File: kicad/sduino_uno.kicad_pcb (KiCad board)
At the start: 2 copper layers, 68.6 x 53.3 mm, 51 parts, among them J1 Conn_01x04, J2 Conn_01x02, Q1 FDN340P, U1 NCP1117-5.0_SOT223, U2 NCP1117-3.3_SOT223, U3 CH340G, U4 STM8S105K_LQFP32, U5 LM358, U6 STM8S105K_UFQFPN32, X1 Jack-DC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

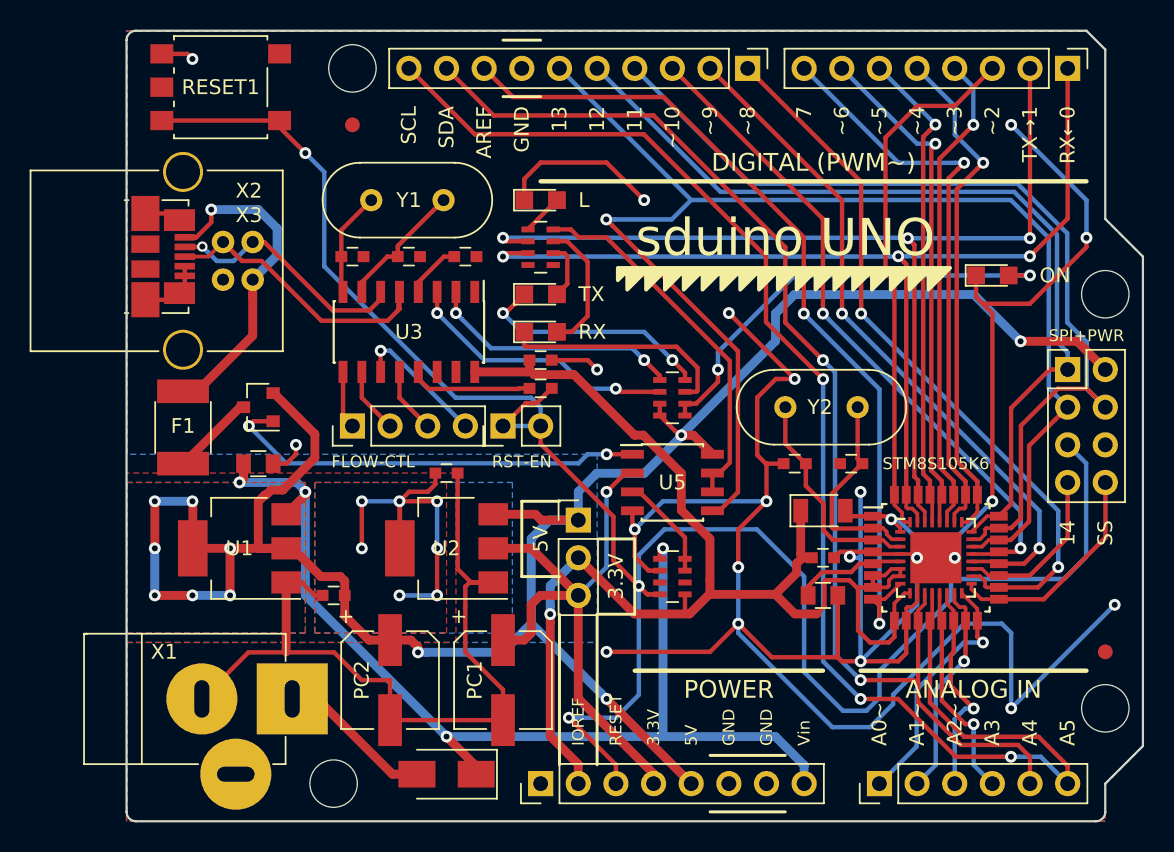
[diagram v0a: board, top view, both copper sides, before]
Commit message: revision 2017-10-08 - fix major error in TX/RX wiring (LEDs were connected in series) - improve ground fill surrounding crystals - rename IO14 to IO23 - add some pin numbers on the back side - update documentation
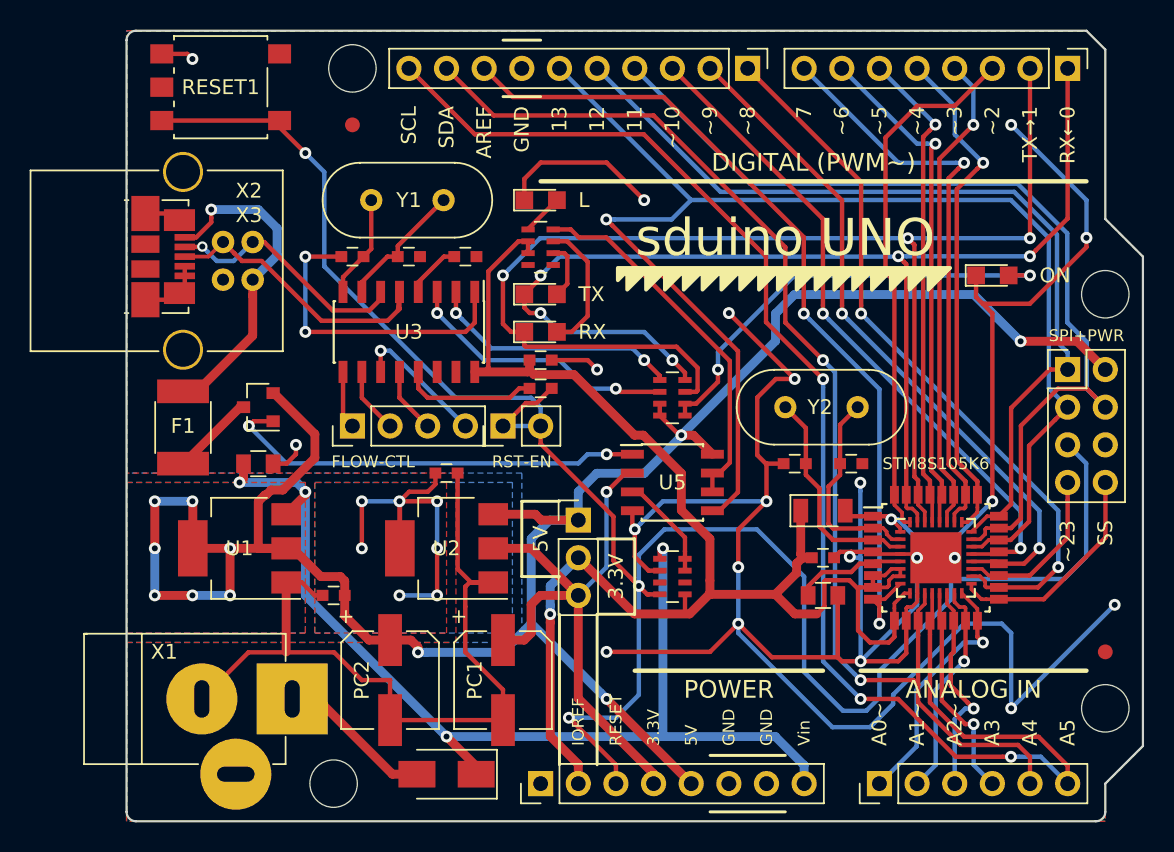
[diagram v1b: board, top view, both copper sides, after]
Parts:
- turned C2 to 180 degrees
- turned C5 to 180 degrees
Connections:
- net /IO14 renamed /IO23
- net /SS renamed /IO24/SS
- LED_RX1 pad 1: Net-(LED_RX1-Pad1) -> /IO1/TX
- LED_TX1 pad 1: Net-(LED_TX1-Pad1) -> /IO0/RX
- RN2 pad 2: /IO1/TX -> /MCUVCC
- RN2 pad 3: /IO0/RX -> /MCUVCC
- RN3 pad 7: Net-(LED_RX1-Pad1) -> /IO1/TX
- RN3 pad 8: Net-(LED_TX1-Pad1) -> /IO0/RX
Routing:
- net GND: track 264.6 -> 286.5 mm, vias 21 -> 23
- net /IO1/TX: track 68.4 -> 88.3 mm
- net Net-(LED_TX1-Pad1): track 16.4 -> 0.00 mm, vias 2 -> 0
- net Net-(LED_RX1-Pad1): track 15.6 -> 0.00 mm
- net /IO0/RX: track 69.8 -> 81.7 mm, vias 3 -> 5
- net /MCUVCC: track 92.4 -> 104.2 mm
- net Net-(C10-Pad1): track 8.26 -> 9.15 mm
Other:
- board text added: "15"
- board text added: "16"
- board text added: "17"
- board text added: "18"
- board text added: "19"
- board text added: "2017-10-08"
- board text added: "22"
- board text added: "24"
- board text added: "~~23"
- board text removed: "2017-10-01"

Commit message: board revision 2017-10-10 (minor PCB changes) - optimized ground fills - reduced thermal relief around the regulators' thermal pads
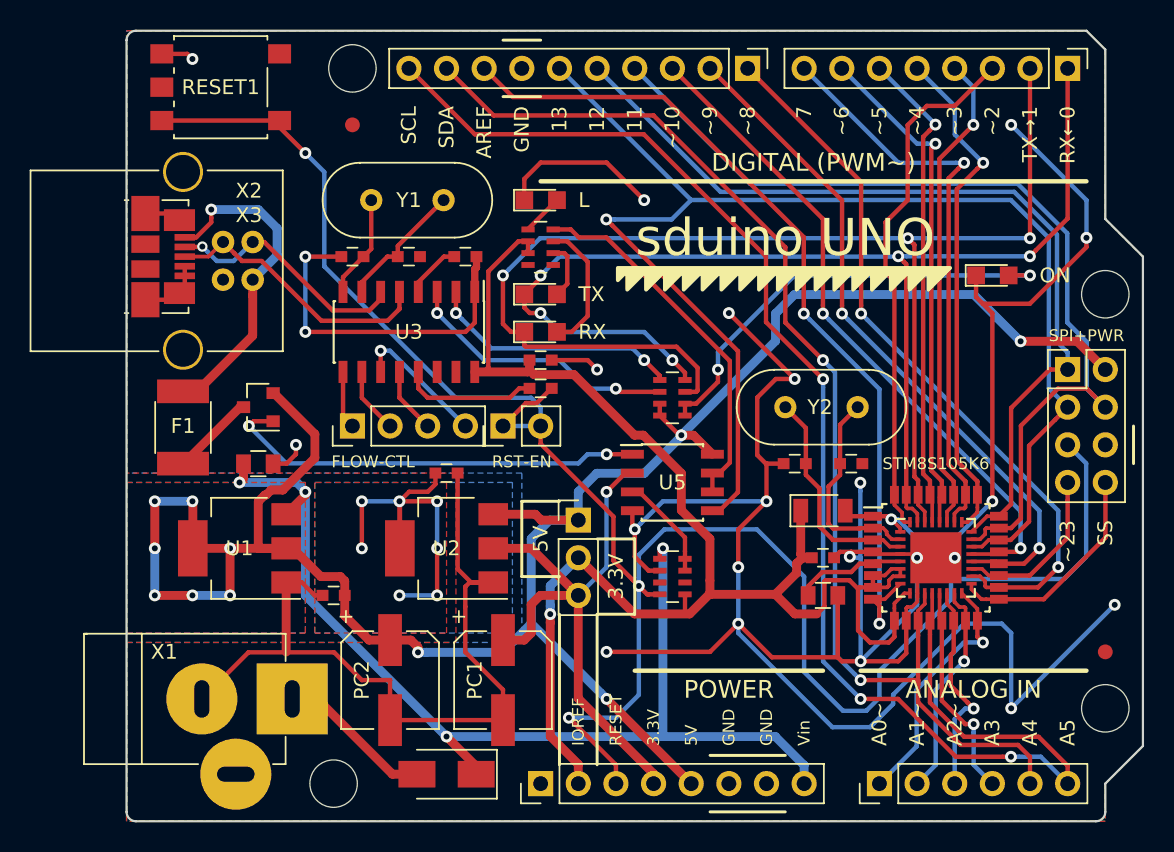
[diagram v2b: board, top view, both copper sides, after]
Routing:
- net GND: track 286.5 -> 288.9 mm
- net /D+: track 20.0 -> 18.7 mm
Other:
- board text added: "2017-10-10"
- board text removed: "2017-10-08"
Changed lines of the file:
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@@
     (area 114.224999 76.124999 182.955001 129.615001)
     (thickness 1.6)
-    (drawings 111)
-    (tracks 916)
+    (drawings 112)
+    (tracks 920)
     (zones 0)
     (modules 51)
@@
     (title "sduino UNO")
     (date 2017-09-15)
-    (rev 2017-10-08)
+    (rev 2017-10-10)
     (company "Benedikt Freisen")
     (comment 1 "see http://creativecommons.org/licenses/by-sa/2.5/")
@@
     (mod_text_size 1 1)
     (mod_text_width 0.15)
-    (pad_size 1.725 1.725)
+    (pad_size 2 3.8)
     (pad_drill 0)
     (pad_to_mask_clearance 0.2)
@@
     (visible_elements FFFFFF7F)
     (pcbplotparams
-      (layerselection 0x00030_80000001)
+      (layerselection 0x010f0_80000001)
       (usegerberextensions false)
       (excludeedgelayer true)
@@
       (outputformat 1)
       (mirror false)
-      (drillshape 1)
+      (drillshape 0)
       (scaleselection 1)
-      (outputdirectory ""))
+      (outputdirectory gerber))
   )
   (net 0 "")
@@
     (fp_line (start 1.85 -3.35) (end 1.85 3.35) (layer F.Fab) (width 0.1))
     (pad 2 smd rect (at 3.15 0 180) (size 2 3.8) (layers F.Cu F.Paste F.Mask)
-      (net 14 +5V))
+      (net 14 +5V) (thermal_width 1.2))
     (pad 2 smd rect (at -3.15 0 180) (size 2 1.5) (layers F.Cu F.Paste F.Mask)
       (net 14 +5V))
@@
     (fp_line (start 1.85 -3.35) (end 1.85 3.35) (layer F.Fab) (width 0.1))
     (pad 2 smd rect (at 3.15 0 180) (size 2 3.8) (layers F.Cu F.Paste F.Mask)
-      (net 15 +3V3))
+      (net 15 +3V3) (thermal_width 1.2))
     (pad 2 smd rect (at -3.15 0 180) (size 2 1.5) (layers F.Cu F.Paste F.Mask)
       (net 15 +3V3))
@@
     )
   )
+  (gr_line (start 182.245 102.87) (end 182.245 105.41) (layer F.SilkS) (width 0.2))
   (gr_text 19 (at 133.35 80.645) (layer B.SilkS)
     (effects (font (size 1 1) (thickness 0.15)) (justify mirror))
@@
     (effects (font (size 1 1) (thickness 0.15)) (justify left mirror))
   )
-  (gr_text 2017-10-08 (at 171.45 91.44) (layer B.SilkS)
+  (gr_text 2017-10-10 (at 171.45 91.44) (layer B.SilkS)
     (effects (font (size 1.5 1.5) (thickness 0.3)) (justify left mirror))
   )
@@
   (gr_line (start 114.935 129.54) (end 179.705 129.54) (layer Edge.Cuts) (width 0.15))
   (gr_line (start 114.3 76.835) (end 114.3 128.905) (layer Edge.Cuts) (width 0.15))
+  (segment (start 137.91 92.176048) (end 137.91 91.44) (width 0.5) (layer F.Cu) (net 1))
+  (segment (start 137.795 92.291048) (end 137.91 92.176048) (width 0.5) (layer F.Cu) (net 1))
+  (segment (start 137.795 93.82) (end 137.795 92.291048) (width 0.5) (layer F.Cu) (net 1))
   (segment (start 163.814278 111.744278) (end 163.814278 107.261686) (width 0.3) (layer B.Cu) (net 1))
   (segment (start 163.814278 107.261686) (end 163.814278 106.696001) (width 0.3) (layer B.Cu) (net 1))
@@
   (via (at 171.457525 122.984562) (size 0.8) (drill 0.4) (layers F.Cu B.Cu) (net 24))
   (segment (start 171.457525 125.737525) (end 171.457525 123.550247) (width 0.3) (layer B.Cu) (net 24))
+  (segment (start 163.83 120.015) (end 167.71 120.015) (width 0.3) (layer F.Cu) (net 25))
+  (segment (start 167.71 120.015) (end 167.71 120.331982) (width 0.3) (layer F.Cu) (net 25))
   (segment (start 168.16 114.16) (end 168.16 114.874998) (width 0.25) (layer F.Cu) (net 25))
   (segment (start 168.16 114.874998) (end 167.71 115.324998) (width 0.25) (layer F.Cu) (net 25))
@@
   (segment (start 162.09934 99.23434) (end 162.09934 118.28434) (width 0.3) (layer B.Cu) (net 25))
   (segment (start 163.430001 119.615001) (end 163.83 120.015) (width 0.3) (layer B.Cu) (net 25))
-  (segment (start 163.83 120.015) (end 167.393018 120.015) (width 0.3) (layer F.Cu) (net 25))
-  (segment (start 167.393018 120.015) (end 167.71 120.331982) (width 0.3) (layer F.Cu) (net 25))
   (via (at 163.83 120.015) (size 0.8) (drill 0.4) (layers F.Cu B.Cu) (net 25))
   (segment (start 158.75 95.885) (end 161.29 98.425) (width 0.3) (layer F.Cu) (net 25))
@@
   (segment (start 165.1 115) (end 164.66 114.56) (width 0.3) (layer F.Cu) (net 33))
   (via (at 165.1 116.205) (size 0.8) (drill 0.4) (layers F.Cu B.Cu) (net 33))
-  (segment (start 166.11 107.51) (end 166.11 93.099533) (width 0.3) (layer F.Cu) (net 34))
-  (segment (start 166.11 93.099533) (end 165.51 92.499533) (width 0.3) (layer F.Cu) (net 34))
-  (segment (start 165.51 92.499533) (end 165.51 83.41) (width 0.3) (layer F.Cu) (net 34))
-  (segment (start 165.51 83.41) (end 167.650509 81.269491) (width 0.3) (layer F.Cu) (net 34))
-  (segment (start 167.650509 81.269491) (end 170.190509 81.269491) (width 0.3) (layer F.Cu) (net 34))
-  (segment (start 170.190509 81.269491) (end 172.72 78.74) (width 0.3) (layer F.Cu) (net 34))
+  (segment (start 165.51 92.499533) (end 166.11 93.099533) (width 0.3) (layer F.Cu) (net 34))
+  (segment (start 165.51 89.125) (end 165.51 92.499533) (width 0.3) (layer F.Cu) (net 34))
+  (segment (start 167.005 87.63) (end 165.51 89.125) (width 0.3) (layer F.Cu) (net 34))
+  (segment (start 167.005 82.563709) (end 167.005 87.63) (width 0.3) (layer F.Cu) (net 34))
+  (segment (start 166.11 93.099533) (end 166.11 107.51) (width 0.3) (layer F.Cu) (net 34))
+  (segment (start 168.299218 81.269491) (end 167.005 82.563709) (width 0.3) (layer F.Cu) (net 34))
+  (segment (start 170.190509 81.269491) (end 168.299218 81.269491) (width 0.3) (layer F.Cu) (net 34))
+  (segment (start 172.72 78.74) (end 170.190509 81.269491) (width 0.3) (layer F.Cu) (net 34))
   (segment (start 172.747499 78.767499) (end 172.72 78.74) (width 0.3) (layer F.Cu) (net 34))
   (segment (start 167.16 109.36) (end 166.785 109.36) (width 0.25) (layer F.Cu) (net 34))
@@
   (segment (start 132.715 94.97) (end 131.914988 95.770012) (width 0.3) (layer F.Cu) (net 58))
   (segment (start 122.089999 91.734999) (end 121.569999 91.214999) (width 0.3) (layer F.Cu) (net 58))
-  (segment (start 132.614999 95.070001) (end 132.715 93.82) (width 0.3) (layer F.Cu) (net 58))
   (segment (start 123.414801 91.734999) (end 122.089999 91.734999) (width 0.3) (layer F.Cu) (net 58))
   (segment (start 132.715 93.82) (end 132.715 94.97) (width 0.3) (layer F.Cu) (net 58))
@@
     (min_thickness 0.254)
     (keepout (tracks allowed) (vias allowed) (copperpour not_allowed))
-    (fill (arc_segments 16) (thermal_gap 0.508) (thermal_bridge_width 0.508))
+    (fill yes (arc_segments 16) (thermal_gap 0.508) (thermal_bridge_width 0.508))
     (polygon
       (pts
@@
     (min_thickness 0.254)
     (keepout (tracks allowed) (vias allowed) (copperpour not_allowed))
-    (fill (arc_segments 16) (thermal_gap 0.508) (thermal_bridge_width 0.508))
+    (fill yes (arc_segments 16) (thermal_gap 0.508) (thermal_bridge_width 0.508))
     (polygon
       (pts
@@
       )
     )
+  )
+  (zone (net 0) (net_name "") (layer F.Cu) (hatch edge 0.508)
+    (connect_pads (clearance 0.5))
+    (min_thickness 0.254)
+    (keepout (tracks allowed) (vias allowed) (copperpour not_allowed))
+    (fill yes (arc_segments 16) (thermal_gap 0.508) (thermal_bridge_width 0.508))
+    (polygon
+      (pts
+        (xy 130.81 88.265) (xy 134.62 88.265) (xy 132.08 90.805) (xy 130.81 90.805)
+      )
+    )
+  )
+  (zone (net 0) (net_name "") (layer F.Cu) (hatch edge 0.508)
+    (connect_pads (clearance 0.5))
+    (min_thickness 0.254)
+    (keepout (tracks allowed) (vias allowed) (copperpour not_allowed))
+    (fill yes (arc_segments 16) (thermal_gap 0.508) (thermal_bridge_width 0.508))
+    (polygon
+      (pts
+        (xy 135.89 91.44) (xy 135.89 93.345) (xy 138.43 93.345) (xy 138.43 91.44)
+      )
+    )
+  )
+  (zone (net 0) (net_name "") (layer F.Cu) (hatch edge 0.508)
+    (connect_pads (clearance 0.5))
+    (min_thickness 0.254)
+    (keepout (tracks allowed) (vias allowed) (copperpour not_allowed))
+    (fill yes (arc_segments 16) (thermal_gap 0.508) (thermal_bridge_width 0.508))
+    (polygon
+      (pts
+        (xy 139.7 102.87) (xy 139.7 115.57) (xy 144.78 115.57) (xy 144.78 102.87)
+      )
+    )
+  )
+  (zone (net 0) (net_name "") (layer F.Cu) (hatch edge 0.508)
+    (connect_pads (clearance 0.5))
+    (min_thickness 0.254)
+    (keepout (tracks allowed) (vias allowed) (copperpour not_allowed))
+    (fill yes (arc_segments 16) (thermal_gap 0.508) (thermal_bridge_width 0.508))
+    (polygon
+      (pts
+        (xy 162.56 78.74) (xy 167.64 83.82) (xy 170.18 83.82) (xy 170.18 78.74)
+      )
+    )

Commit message: board revision 2017-11-15 (minor corrections and clarifications)
- use more precise names for some components
- adjust footprint of DC jack to better fit the DC jack
- adjust thermal relief around pads of 0603 components
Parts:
- SPI_PWR1: value Conn_02x03_Odd_Even -> Conn_02x04_Odd_Even
- U4: value STM8S105K_LQFP32 -> STM8S105K6T6C_LQFP32
- U6: value STM8S105K_UFQFPN32 -> STM8S105K6U6A_UFQFPN32
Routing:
- net GND: track 288.9 -> 290.8 mm
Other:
- board text added: "2017-11-15"
- board text removed: "2017-10-10"
